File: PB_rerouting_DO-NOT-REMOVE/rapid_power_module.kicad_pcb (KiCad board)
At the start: 4 copper layers, 80 x 136 mm, 207 parts, among them J1 Conn_02x04_Top_Bottom, J10 JST-GH 4Pin, J11 SWD Header, J12 SWD Header, J16 USB_C_Receptacle_USB2.0, J17 TC2050, J2 Conn_02x03_Odd_Even, J3 Conn_02x04_Top_Bottom, J4 Conn_02x03_Odd_Even, J6 Molex MicroFit 2x2, J7 Molex MicroFit 2x2, J8 Molex MicroFit 2x2, J9 Conn_02x04_Top_Bottom, Q1 AOSP21321, Q12 AOSP21321, Q4 HiDRV1, Q5 LoDRV1, Q6 HiDRV2, Q7 LoDRV2, SW1 KMR721NGLFS, SW2 KMR721NGLFS, U1 BQ25756RRVR, U10 L7805, U11 MCP2562-E-SN, U12 STM32F105RCTx, U13 AZ1117I-3.3, U14 TPD4E1U06, U15 TPD4E1U06, U2 CYPD3177-24LQ, U3 BQ76952PFBR, Y3 8MHz 12pF

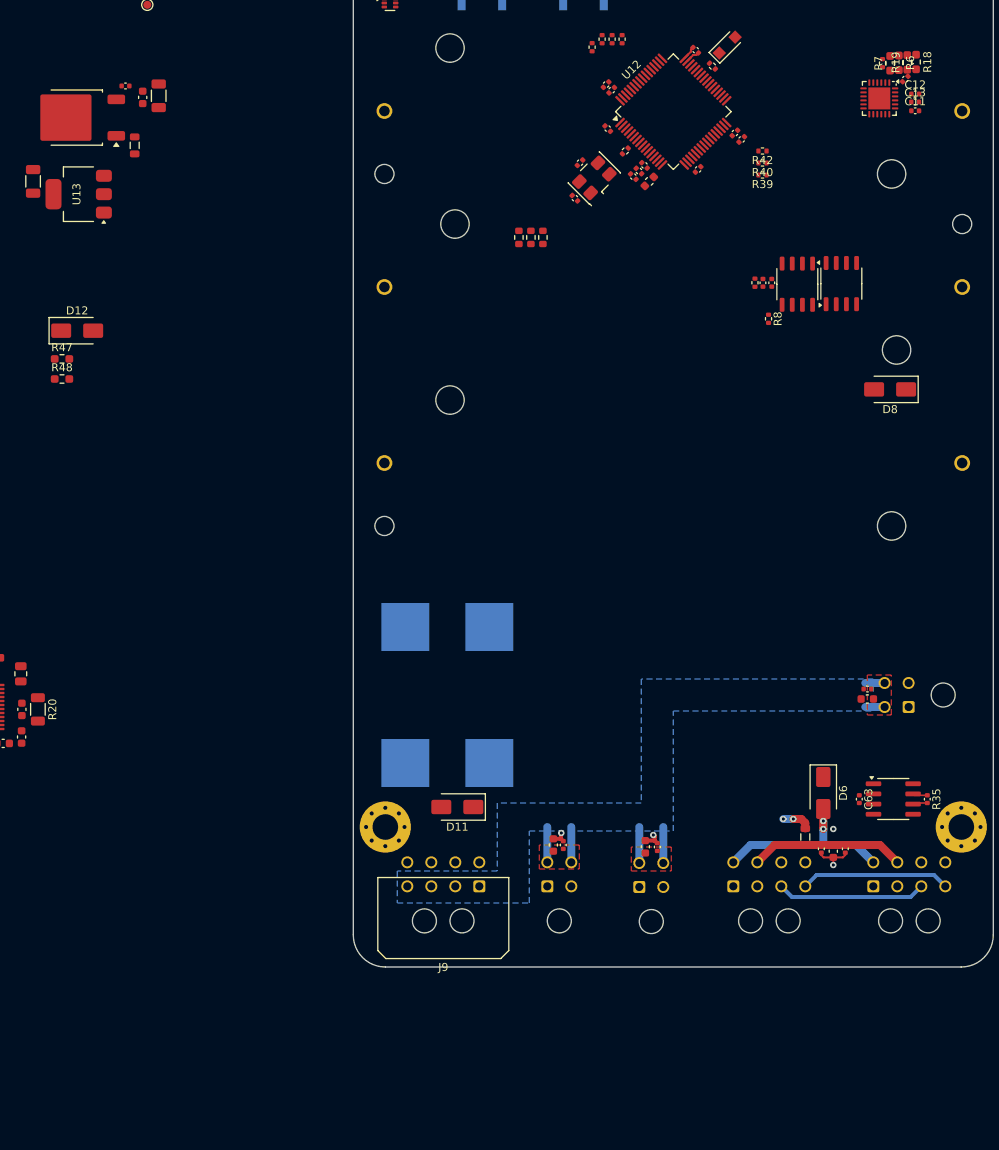
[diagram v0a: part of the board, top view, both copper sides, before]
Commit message: scematic adaptations and routing
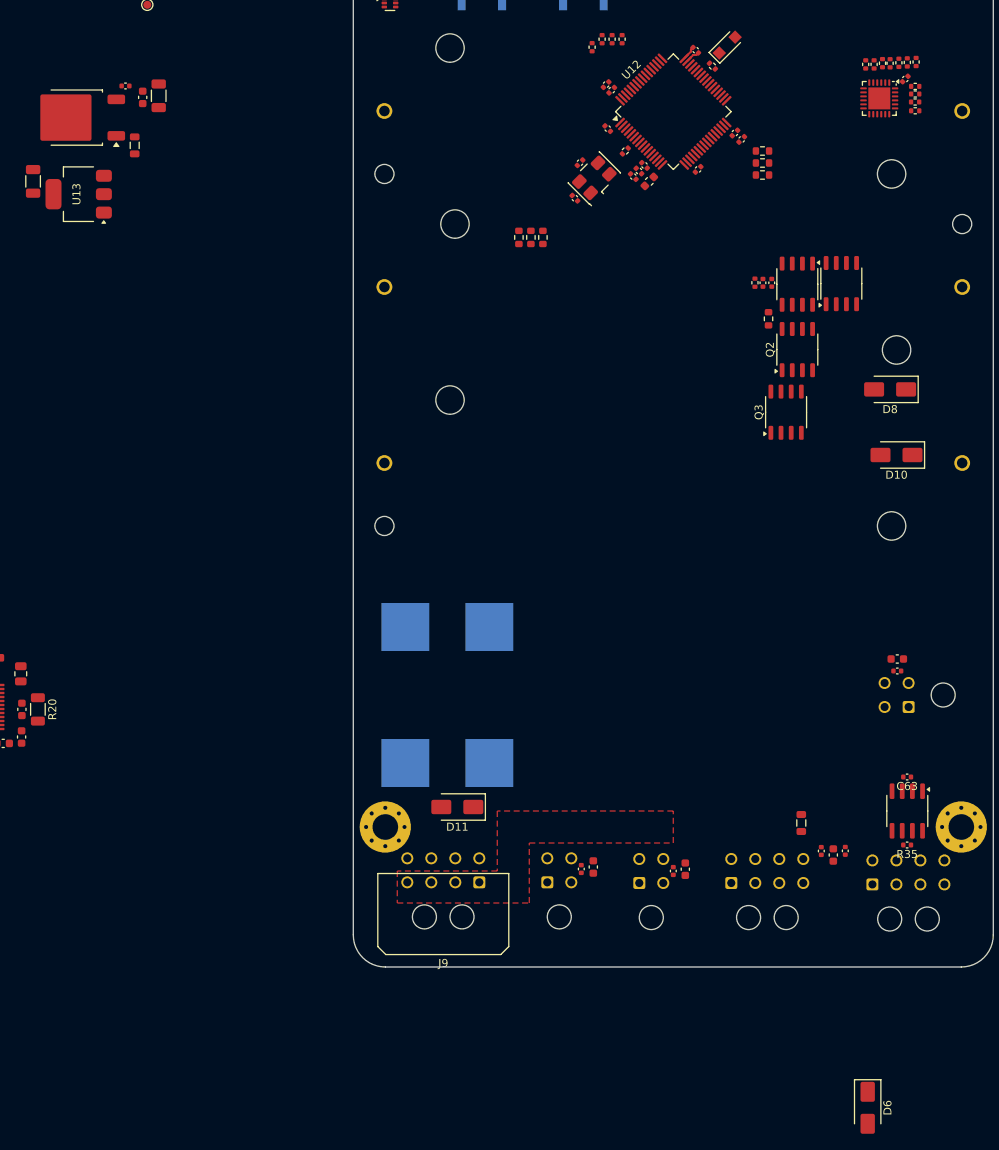
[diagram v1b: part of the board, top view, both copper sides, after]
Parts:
- removed D12: ~, Diode_SMD:D_SMA
- removed R47: dnp, Resistor_SMD:R_0603_1608Metric_Pad0.98x0.95mm_HandSolder
- removed R48: 0R, Resistor_SMD:R_0603_1608Metric_Pad0.98x0.95mm_HandSolder
- added D10: ~, Diode_SMD:D_SMA, F.Cu at (162.9, 94.0)
- added Q2: AOSP21321, Package_SO:SO-8_3.9x4.9mm_P1.27mm, F.Cu at (150.5, 80.8)
- added Q3: AOSP21321, Package_SO:SO-8_3.9x4.9mm_P1.27mm, F.Cu at (149.1, 88.7)
- added R10: 5k1, Resistor_SMD:R_0402_1005Metric, F.Cu at (165.2, 47.9)
- added R13: 10k, Resistor_SMD:R_0402_1005Metric, F.Cu at (159.0, 45.2)
- added R9: 1k, Resistor_SMD:R_0402_1005Metric, F.Cu at (160.1, 45.2)
- C11, C12, C13: footprint Capacitor_SMD:C_0402_1005Metric -> Resistor_SMD:R_0402_1005Metric
- R18, R7: value dnp -> 5k1; footprint Resistor_SMD:R_0603_1608Metric_Pad0.98x0.95mm_HandSolder -> Resistor_SMD:R_0402_1005Metric
- R19, R6: value 0R -> 5k1; footprint Resistor_SMD:R_0603_1608Metric_Pad0.98x0.95mm_HandSolder -> Resistor_SMD:R_0402_1005Metric
- R39: value 4k7 -> 4.7k; footprint Resistor_SMD:R_0402_1005Metric -> Resistor_SMD:R_0603_1608Metric
- R40, R42, R8: footprint Resistor_SMD:R_0402_1005Metric -> Resistor_SMD:R_0603_1608Metric
- moved D6 39.7 mm to (159.3, 175.6)
- moved C63 6.59 mm to (164.2, 134.2), turned to 180 degrees
- moved R35 6.26 mm to (164.2, 142.8), turned to 180 degrees
- moved C88 6.25 mm to (163.0, 119.5), turned to 0 degrees
- moved C84 5.73 mm to (136.5, 145.8), turned to -90 degrees
- moved C86 5.71 mm to (125.0, 145.5), turned to -90 degrees
- moved C89 4.36 mm to (163.0, 121.0), turned to 0 degrees
- moved C87 3.75 mm to (123.5, 145.8), turned to -90 degrees
- moved C85 3.61 mm to (135.0, 146.0), turned to -90 degrees
- moved U11 2.30 mm to (164.2, 138.5), turned to -90 degrees
- moved FB2 1.82 mm to (151.0, 140.0)
- moved J6 0.50 mm to (130.8, 147.5)
- moved J8 0.50 mm to (119.2, 147.4)
- moved J9 0.50 mm to (110.8, 147.4)
- moved J3 0.48 mm to (142.2, 147.5)
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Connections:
- C10 pad 2: Net-(D12-A) -> Net-(Q1-G)
- C11 pad 1: PD_VDDD -> 3.3V PD
- C12 pad 1: PD_VDDD -> 3.3V PD
- C13 pad 1: PD_VDDD -> 3.3V PD
- C9 pad 2: Net-(D12-A) -> Net-(Q1-G)
- Q1 pad 1: Net-(D12-K) -> USB_PD_OUT
- Q1 pad 2: Net-(D12-K) -> USB_PD_OUT
- Q1 pad 3: Net-(D12-K) -> USB_PD_OUT
- Q1 pad 4: Net-(D12-A) -> Net-(Q1-G)
- Q1 pad 5: USB_PD_OUT -> Net-(Q1-D-Pad5)
- Q1 pad 6: USB_PD_OUT -> Net-(Q1-D-Pad5)
- Q1 pad 7: USB_PD_OUT -> Net-(Q1-D-Pad5)
- Q1 pad 8: USB_PD_OUT -> Net-(Q1-D-Pad5)
- Q12 pad 1: Net-(D12-K) -> Net-(Q1-D-Pad5)
- Q12 pad 2: Net-(D12-K) -> Net-(Q1-D-Pad5)
- Q12 pad 3: Net-(D12-K) -> Net-(Q1-D-Pad5)
- Q12 pad 4: Net-(D12-A) -> Net-(Q1-G)
- R18 pad 1: PD_VDDD -> 3.3V PD
- R4 pad 2: Net-(D12-A) -> Net-(Q1-G)
- R5 pad 1: Net-(D12-A) -> Net-(Q1-G)
- R6 pad 1: PD_VDDD -> 3.3V PD
- R8 pad 1: Net-(D12-K) -> /VBUS
- R8 pad 2: Net-(D12-A) -> Net-(Q2-G)
- U2 pad 23: PD_VDDD -> 3.3V PD
- U2 pad 6: PD_VDDD -> GND
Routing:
- net charging_voltage: track 24.8 -> 0.00 mm, vias 2 -> 0
- net +VSW: track 22.7 -> 0.00 mm
- net CAN-: track 20.4 -> 0.00 mm
- net main_voltage: track 19.3 -> 0.00 mm
- net CAN_2_L: track 19.0 -> 0.00 mm
- net GND: track 18.8 -> 9.51 mm, vias 6 -> 2
- net Net-(F1-Pad2): track 3.64 -> 0.00 mm, vias 2 -> 0
- net CAN+: track 1.85 -> 0.00 mm
- removed copper zone on B.Cu, net +VSW
